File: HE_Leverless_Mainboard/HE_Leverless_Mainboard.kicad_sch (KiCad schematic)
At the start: 62 parts

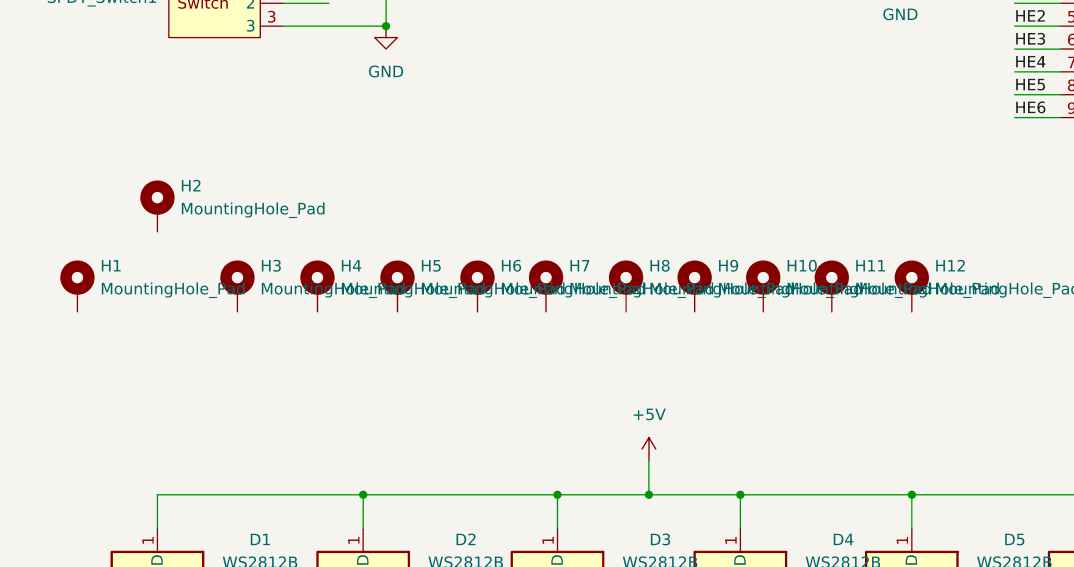
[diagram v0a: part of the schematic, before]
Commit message: Added images
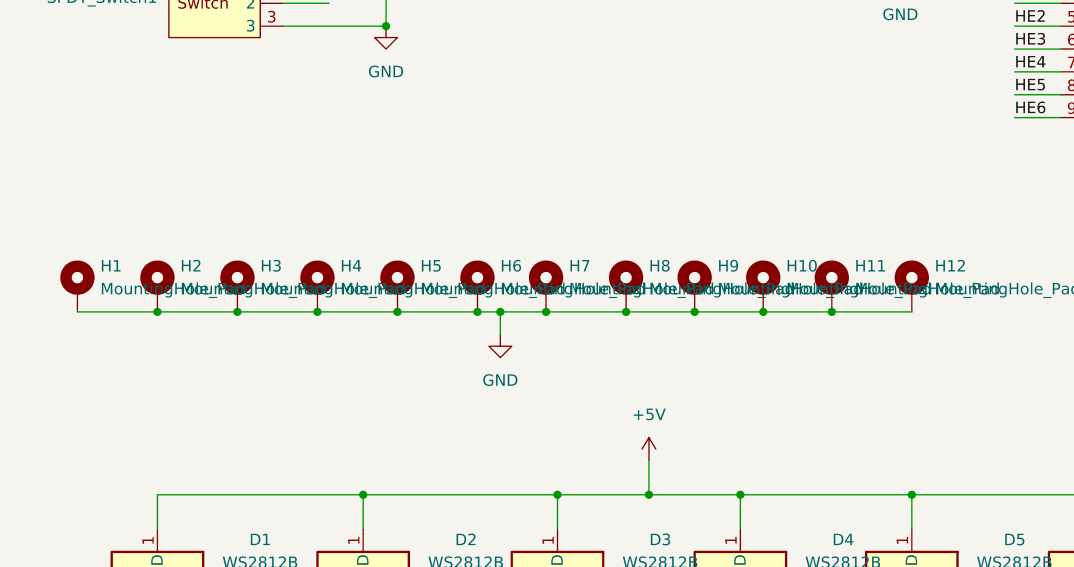
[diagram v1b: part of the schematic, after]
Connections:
- net GND: now also H1.1, H10.1, H11.1, H12.1, H2.1, H3.1, H4.1, H5.1, H6.1, H7.1, H8.1, H9.1
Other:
- moved on the sheet: H2
